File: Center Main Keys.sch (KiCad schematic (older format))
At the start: 4 parts

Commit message: 3 Board Schematics Complete
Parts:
- added C? (x4): 1n, symbol Device:C
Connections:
- net GND: now also C?.2, C?.2, C?.2, C?.2
- net SHIFT_2_DATA: now also U?.9 (QH)
- net SHIFT_3_DATA: no longer U?.9 (QH)
- net VCC: now also C?.1, C?.1, C?.1, C?.1
- net F5: now reaches U?.1 (B)
- net F4: now reaches U?.15 (A)
- net F6: now reaches U?.2 (C)
- net F7: now reaches U?.3 (D)
- net F8: now reaches U?.4 (E)
- net 4: now reaches U?.5 (F)
- net 5: now reaches U?.6 (G)
- net 6: now reaches U?.7 (H)
- net 8: now reaches U?.1 (B)
- net 7: now reaches U?.15 (A)
- net 9: now reaches U?.2 (C)
- net E: now reaches U?.3 (D)
- net R: now reaches U?.4 (E)
- net T: now reaches U?.5 (F)
- net Y: now reaches U?.6 (G)
- net U: now reaches U?.7 (H)
- net D: now reaches U?.1 (B)
- net I: now reaches U?.15 (A)
- net F: now reaches U?.2 (C)
- net G: now reaches U?.3 (D)
- net H: now reaches U?.4 (E)
- net J: now reaches U?.5 (F)
- net K: now reaches U?.6 (G)
- net C: now reaches U?.7 (H)
- net B: now reaches U?.1 (B)
- net V: now reaches U?.15 (A)
- net N: now reaches U?.2 (C)
- net M: now reaches U?.3 (D)
- net ,: now reaches U?.4 (E)
- net SP: now reaches U?.5 (F)

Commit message: Schematic completed first draft
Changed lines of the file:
@@
 $Descr A4 11693 8268
 encoding utf-8
-Sheet 4 12
+Sheet 4 18
 Title ""
 Date ""
@@
 Entry Wire Line
 	6150 7450 6250 7550
-Wire Bus Line
-	6350 6150 6250 6150
-Wire Bus Line
-	6350 6050 6250 6050
-Connection ~ 6350 6050
-Wire Bus Line
-	6350 6050 6350 6150
-Wire Bus Line
-	6350 5950 6250 5950
-Connection ~ 6350 5950
-Wire Bus Line
-	6350 5950 6350 6050
-Wire Bus Line
-	6350 5850 6250 5850
-Connection ~ 6350 5850
-Wire Bus Line
-	6350 5850 6350 5950
-Wire Bus Line
-	6350 5750 6250 5750
-Connection ~ 6350 5750
-Wire Bus Line
-	6350 5750 6350 5850
-Wire Bus Line
-	6350 5650 6250 5650
-Connection ~ 6350 5650
-Wire Bus Line
-	6350 5650 6350 5750
-Wire Bus Line
-	6350 5550 6250 5550
-Connection ~ 6350 5550
-Wire Bus Line
-	6350 5550 6350 5650
-Wire Bus Line
-	6350 5450 6250 5450
-Connection ~ 6350 5450
-Wire Bus Line
-	6350 5450 6350 5550
 Entry Wire Line
 	1950 2850 2050 2750
@@
 Entry Wire Line
 	7950 3350 8050 3250
-Wire Bus Line
-	6250 6250 6450 6250
-Wire Bus Line
-	6250 6350 6450 6350
-Wire Bus Line
-	6250 6450 6450 6450
-Wire Bus Line
-	6250 6550 6450 6550
-Wire Bus Line
-	6250 6650 6450 6650
-Wire Bus Line
-	6250 6750 6450 6750
-Wire Bus Line
-	6250 6850 6450 6850
-Wire Bus Line
-	6250 6950 6450 6950
-Wire Bus Line
-	6450 6950 6450 6850
-Connection ~ 6450 6250
-Connection ~ 6450 6350
-Wire Bus Line
-	6450 6350 6450 6250
-Connection ~ 6450 6450
-Wire Bus Line
-	6450 6450 6450 6350
-Connection ~ 6450 6550
-Wire Bus Line
-	6450 6550 6450 6450
-Connection ~ 6450 6650
-Wire Bus Line
-	6450 6650 6450 6550
-Connection ~ 6450 6750
-Wire Bus Line
-	6450 6750 6450 6650
-Connection ~ 6450 6850
-Wire Bus Line
-	6450 6850 6450 6750
-Wire Bus Line
-	6250 7050 6550 7050
-Wire Bus Line
-	6250 7150 6550 7150
-Wire Bus Line
-	6250 7250 6550 7250
-Wire Bus Line
-	6250 7350 6550 7350
-Wire Bus Line
-	6250 7450 6550 7450
-Wire Bus Line
-	6250 7550 6550 7550
-Wire Bus Line
-	6550 7550 6550 7450
-Connection ~ 6550 7050
-Connection ~ 6550 7150
-Wire Bus Line
-	6550 7150 6550 7050
-Connection ~ 6550 7250
-Wire Bus Line
-	6550 7250 6550 7150
-Connection ~ 6550 7350
-Wire Bus Line
-	6550 7350 6550 7250
-Connection ~ 6550 7450
-Wire Bus Line
-	6550 7450 6550 7350
 $Sheet
 S 2700 5500 1050 1000
@@
 Wire Wire Line
 	10100 1500 10600 1500
-Wire Bus Line
-	1950 4350 6250 4350
-Wire Bus Line
-	6350 4250 3950 4250
-Wire Bus Line
-	6350 4250 6350 5450
-Wire Bus Line
-	6450 4150 5950 4150
-Wire Bus Line
-	6450 4150 6450 6250
-Wire Bus Line
-	6550 4150 7950 4150
-Wire Bus Line
-	6550 4150 6550 7050
 Wire Wire Line
 	1000 1100 1400 1100
@@
 Wire Wire Line
 	9350 1200 9350 3450
+Connection ~ 3950 4300
 Wire Bus Line
-	7950 2850 7950 4150
+	3950 4300 1950 4300
+Connection ~ 5950 4300
 Wire Bus Line
-	1950 2850 1950 4350
+	5950 4300 3950 4300
 Wire Bus Line
-	6250 4350 6250 5350
+	5950 4300 6250 4300
 Wire Bus Line
-	3950 2850 3950 4250
+	7950 2850 7950 4300
 Wire Bus Line
-	5950 2850 5950 4150
+	1950 2850 1950 4300
+Wire Bus Line
+	3950 2850 3950 4300
+Wire Bus Line
+	5950 2850 5950 4300
+Wire Bus Line
+	6250 4300 6250 7550
+Connection ~ 6250 4300
+Wire Bus Line
+	6250 4300 7950 4300
 $EndSCHEMATC

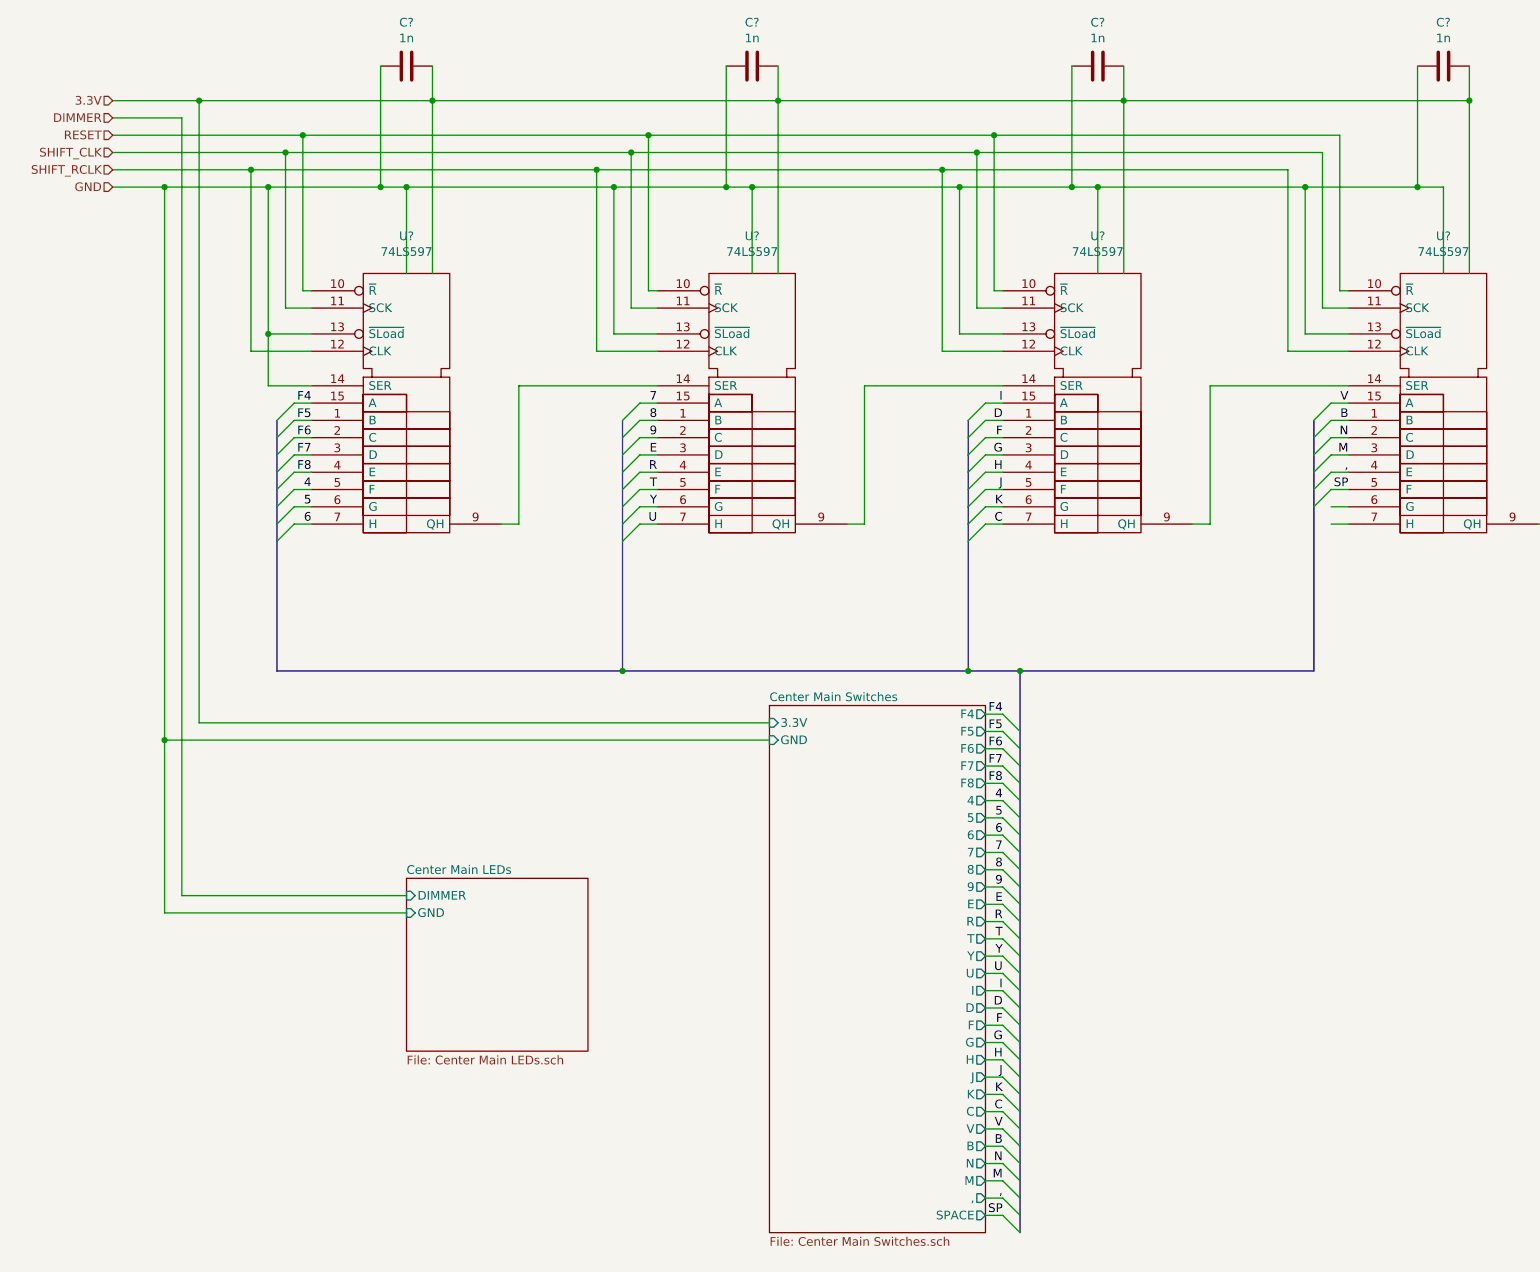
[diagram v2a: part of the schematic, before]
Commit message: Fixed PISO Shift Register Wiring
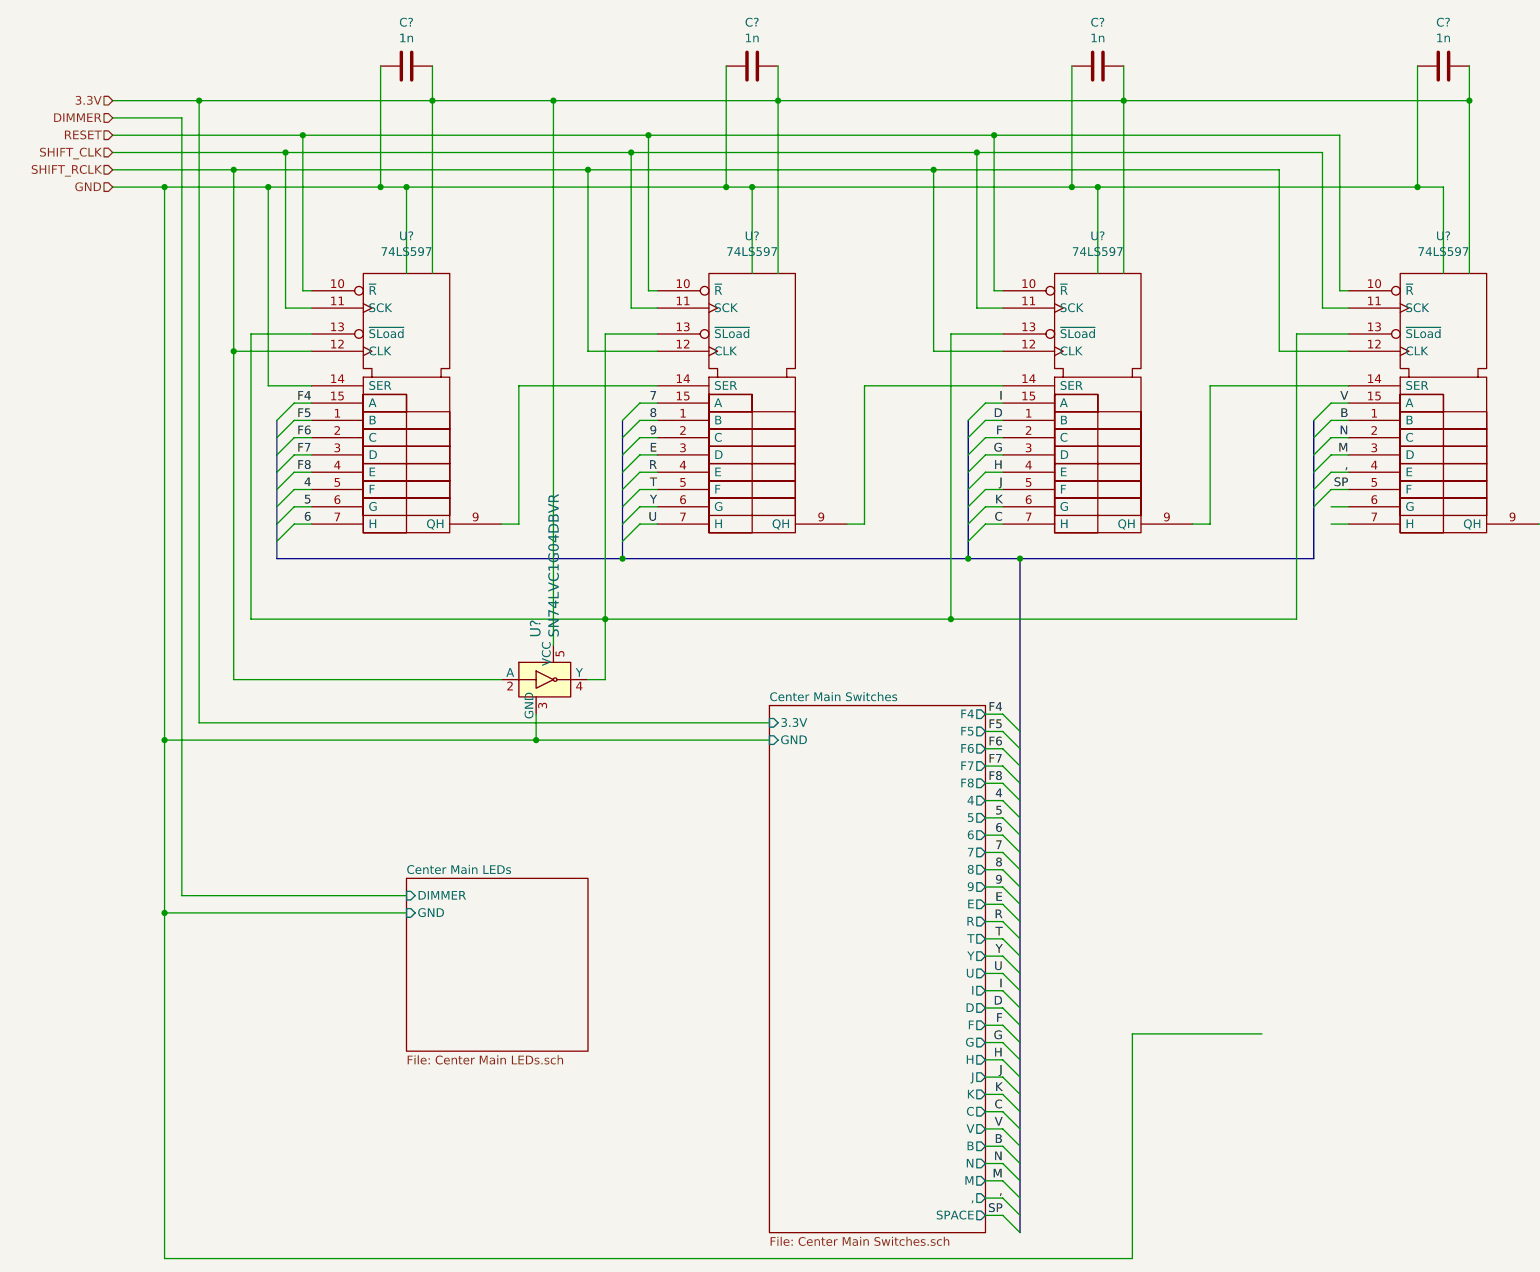
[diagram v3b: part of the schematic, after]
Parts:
- added U?: SN74LVC1G04DBVR, digikey-footprints:SOT-753, symbol dk_Logic-Gates-and-Inverters:SN74LVC1G04DBVR
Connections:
- net GND: now also U?.3 (GND); no longer U?.13 (~SLoad), U?.13 (~SLoad), U?.13 (~SLoad), U?.13 (~SLoad)
- net SHIFT_RCLK: now also U?.2 (A)
- net VCC: now also U?.5 (VCC)
- new net: U?.13 (~SLoad), U?.13 (~SLoad), U?.13 (~SLoad), U?.13 (~SLoad), U?.4 (Y)
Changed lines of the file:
@@
 	2700 1500 2700 2000
-Wire Wire Line
-	2700 1500 3900 1500
 Wire Wire Line
 	4700 1500 4700 2000
 Connection ~ 2700 1500
 Wire Wire Line
-	2850 1000 4850 1000
+	2850 1000 3550 1000
 Wire Wire Line
 	4850 1000 4850 2000
@@
 Connection ~ 4700 1500
 Wire Wire Line
-	6850 1000 8850 1000
-Wire Wire Line
 	8850 1000 8850 2000
 Connection ~ 6850 1000
 Wire Wire Line
 	8700 1500 8700 2000
-Wire Wire Line
-	4700 1500 5900 1500
 Connection ~ 6700 1500
-Wire Wire Line
-	6700 1500 7900 1500
 Wire Wire Line
 	2100 1200 2100 2100
@@
 	8000 2200 8150 2200
 Connection ~ 6000 1300
-Wire Wire Line
-	2150 2350 1900 2350
-Wire Wire Line
-	1900 2350 1900 1500
 Connection ~ 1900 1500
 Wire Wire Line
 	1900 1500 2550 1500
 Wire Wire Line
-	2150 2450 1800 2450
-Wire Wire Line
-	1800 2450 1800 1400
-Connection ~ 1800 1400
-Wire Wire Line
-	4150 2350 3900 2350
-Wire Wire Line
-	3900 2350 3900 1500
-Connection ~ 3900 1500
-Wire Wire Line
-	3900 1500 4550 1500
-Wire Wire Line
-	6150 2350 5900 2350
-Wire Wire Line
-	5900 2350 5900 1500
-Connection ~ 5900 1500
-Wire Wire Line
-	5900 1500 6550 1500
-Wire Wire Line
-	8150 2350 7900 2350
-Wire Wire Line
-	7900 2350 7900 1500
-Connection ~ 7900 1500
-Wire Wire Line
-	7900 1500 8550 1500
-Wire Wire Line
-	7800 1400 7800 2450
-Wire Wire Line
-	7800 2450 8150 2450
-Wire Wire Line
-	1800 1400 3800 1400
-Wire Wire Line
-	6150 2450 5800 2450
-Wire Wire Line
-	5800 2450 5800 1400
-Connection ~ 5800 1400
-Wire Wire Line
-	5800 1400 7800 1400
-Wire Wire Line
-	4150 2450 3800 2450
-Wire Wire Line
-	3800 2450 3800 1400
-Connection ~ 3800 1400
-Wire Wire Line
-	3800 1400 5800 1400
-Wire Wire Line
-	1900 2350 1900 2650
+	1700 2450 1700 1400
+Wire Wire Line
+	7750 1400 7750 2450
+Wire Wire Line
+	5750 2450 5750 1400
+Wire Wire Line
+	3750 2450 3750 1400
 Wire Wire Line
 	1900 2650 2150 2650
-Connection ~ 1900 2350
 $Comp
 L Device:C C?
@@
 Wire Wire Line
 	1000 1300 2000 1300
-Wire Wire Line
-	1000 1400 1800 1400
 Wire Wire Line
 	1000 1500 1300 1500
@@
 	1300 1500 1900 1500
 Wire Wire Line
-	4800 4700 1300 4700
+	4800 4700 3450 4700
 Connection ~ 1300 4700
 Wire Wire Line
@@
 Wire Wire Line
 	9350 1200 9350 3450
-Connection ~ 3950 4300
-Wire Bus Line
-	3950 4300 1950 4300
-Connection ~ 5950 4300
-Wire Bus Line
-	5950 4300 3950 4300
-Wire Bus Line
-	5950 4300 6250 4300
-Wire Bus Line
-	7950 2850 7950 4300
-Wire Bus Line
-	1950 2850 1950 4300
-Wire Bus Line
-	3950 2850 3950 4300
-Wire Bus Line
-	5950 2850 5950 4300
-Wire Bus Line
-	6250 4300 6250 7550
-Connection ~ 6250 4300
-Wire Bus Line
-	6250 4300 7950 4300
+Wire Bus Line
+	1950 3650 3950 3650
+Connection ~ 3950 3650
+Wire Bus Line
+	3950 3650 5950 3650
+Connection ~ 5950 3650
+Wire Bus Line
+	5950 3650 6250 3650
+Connection ~ 6250 3650
+Wire Bus Line
+	6250 3650 7950 3650
+Wire Wire Line
+	1900 1500 1900 2650
+Wire Wire Line
+	2150 2350 1800 2350
+Connection ~ 1700 1400
+Wire Wire Line
+	1700 1400 3750 1400
+Wire Wire Line
+	1700 2450 2150 2450
+Wire Wire Line
+	1000 1400 1700 1400
+Wire Wire Line
+	2700 1500 4550 1500
+Wire Wire Line
+	3850 2350 4150 2350
+Connection ~ 3750 1400
+Wire Wire Line
+	3750 1400 5750 1400
+Wire Wire Line
+	3750 2450 4150 2450
+Wire Wire Line
+	4700 1500 6550 1500
+Connection ~ 5750 1400
+Wire Wire Line
+	5750 1400 7750 1400
+Wire Wire Line
+	5750 2450 6150 2450
+Wire Wire Line
+	5850 2350 6150 2350
+Wire Wire Line
+	6700 1500 8550 1500
+Wire Wire Line
+	7750 2450 8150 2450
+Wire Wire Line
+	7850 2350 8150 2350
+Wire Wire Line
+	7650 6400 6900 6400
+Wire Wire Line
+	6900 6400 6900 7700
+Wire Wire Line
+	6900 7700 1300 7700
+Wire Wire Line
+	1300 7700 1300 5700
+Connection ~ 1300 5700
+Wire Wire Line
+	6850 1000 8850 1000
+$Comp
+L dk_Logic-Gates-and-Inverters:SN74LVC1G04DBVR U?
+U 1 1 5ECE7149
+P 3550 4350
+AR Path="/5E8C755A/5ECE7149" Ref="U?"  Part="1"
+AR Path="/5E8C7194/5ECE7149" Ref="U?"  Part="1"
+F 0 "U?" V 3447 4594 60  0000 L CNN
+F 1 "SN74LVC1G04DBVR" V 3553 4594 60  0000 L CNN
+F 2 "digikey-footprints:SOT-753" H 3750 4550 60  0001 L CNN
+F 3 "http://www.ti.com/general/docs/suppproductinfo.tsp?distId=10&gotoUrl=http%3A%2F%2Fwww.ti.com%2Flit%2Fgpn%2Fsn74lvc1g04" H 3750 4650 60  0001 L CNN
+F 4 "296-11599-1-ND" H 3750 4750 60  0001 L CNN "Digi-Key_PN"
+F 5 "SN74LVC1G04DBVR" H 3750 4850 60  0001 L CNN "MPN"
+F 6 "Integrated Circuits (ICs)" H 3750 4950 60  0001 L CNN "Category"
+F 7 "Logic - Gates and Inverters" H 3750 5050 60  0001 L CNN "Family"
+F 8 "http://www.ti.com/general/docs/suppproductinfo.tsp?distId=10&gotoUrl=http%3A%2F%2Fwww.ti.com%2Flit%2Fgpn%2Fsn74lvc1g04" H 3750 5150 60  0001 L CNN "DK_Datasheet_Link"
+F 9 "/product-detail/en/texas-instruments/SN74LVC1G04DBVR/296-11599-1-ND/385738" H 3750 5250 60  0001 L CNN "DK_Detail_Page"
+F 10 "IC INVERTER 1CH 1-INP SOT23-5" H 3750 5350 60  0001 L CNN "Description"
+F 11 "Texas Instruments" H 3750 5450 60  0001 L CNN "Manufacturer"
+F 12 "Active" H 3750 5550 60  0001 L CNN "Status"
+	1    3550 4350
+	1    0    0    -1
+$EndComp
+Wire Wire Line
+	3250 4350 1700 4350
+Connection ~ 1700 2450
+Connection ~ 3550 1000
+Wire Wire Line
+	3550 1000 4850 1000
+Wire Wire Line
+	3450 4550 3450 4700
+Connection ~ 3450 4700
+Wire Wire Line
+	3450 4700 1300 4700
+Wire Wire Line
+	3750 4350 3850 4350
+Wire Wire Line
+	1700 2450 1700 4350
+Wire Wire Line
+	3550 1000 3550 4150
+Wire Wire Line
+	3850 2350 3850 4000
+Wire Wire Line
+	3850 4000 1800 4000
+Wire Wire Line
+	1800 4000 1800 2350
+Connection ~ 3850 4000
+Wire Wire Line
+	3850 4000 3850 4350
+Wire Wire Line
+	3850 4000 5850 4000
+Wire Wire Line
+	5850 4000 5850 2350
+Wire Wire Line
+	5850 4000 7850 4000
+Wire Wire Line
+	7850 4000 7850 2350
+Connection ~ 5850 4000
+Wire Bus Line
+	7950 2850 7950 3650
+Wire Bus Line
+	5950 2850 5950 3650
+Wire Bus Line
+	3950 2850 3950 3650
+Wire Bus Line
+	1950 2850 1950 3650
+Wire Bus Line
+	6250 3650 6250 7550
 $EndSCHEMATC
